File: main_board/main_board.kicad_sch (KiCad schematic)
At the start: 56 parts, among them J1 USB4105-GF-A-060, J2 Conn_01x06_Pin, Q3 NX3008PBK,215, U1 SSD1306, U2 ESP32-S2-SOLO, U3 TLV62568PDRLT, U4 MCP73832, U5 DW01, U6 8205A, U7 MAX17055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

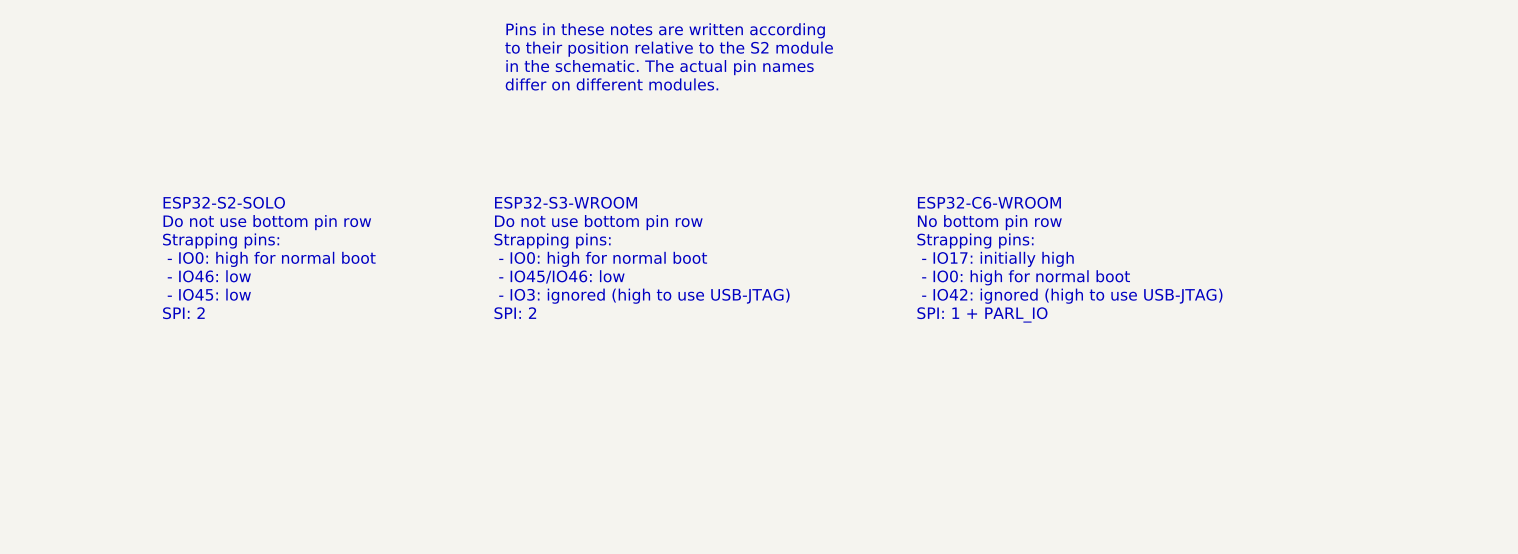
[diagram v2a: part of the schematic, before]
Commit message: Add a note about LP GPIO ranges
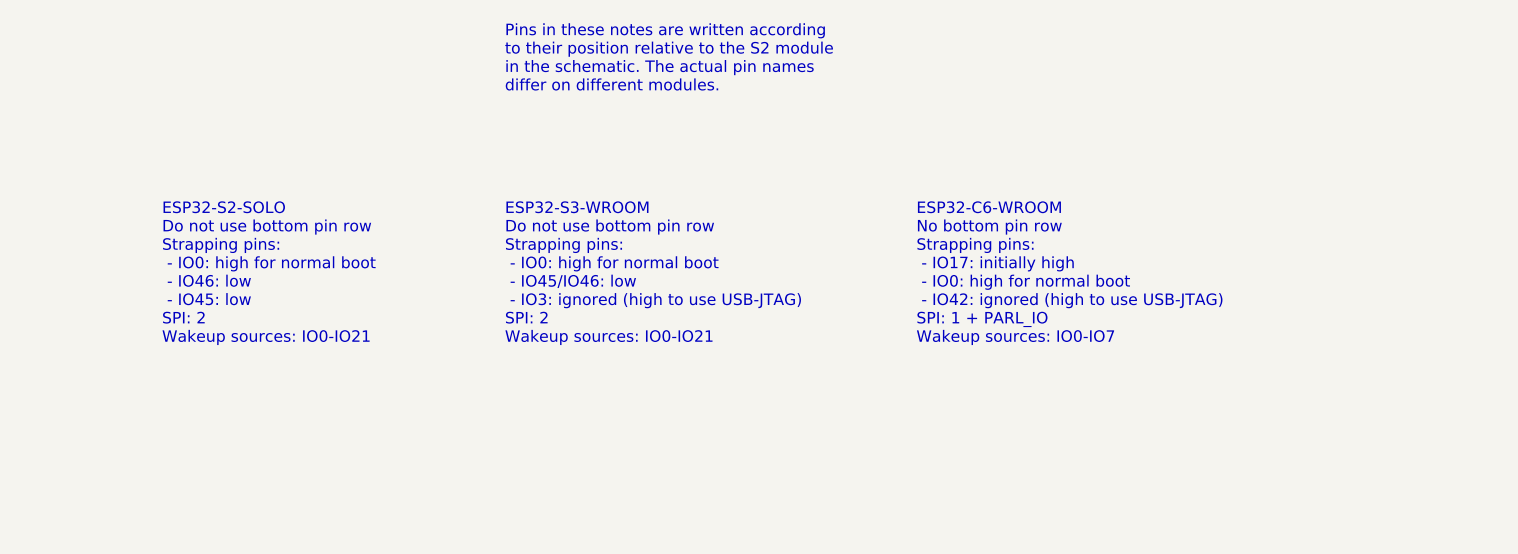
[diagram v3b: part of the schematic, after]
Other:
- note added: "ESP32-C6-WROOM No bottom pin row Strapping pins: - IO17: initially high - IO0: high for normal boot - IO42: ignored (high to use USB-JTAG) SPI: 1 + PARL_IO Wakeup sources: IO0-IO7"
- note added: "ESP32-S2-SOLO Do not use bottom pin row Strapping pins: - IO0: high for normal boot - IO46: low - IO45: low SPI: 2 Wakeup sources: IO0-IO21"
- note added: "ESP32-S3-WROOM Do not use bottom pin row Strapping pins: - IO0: high for normal boot - IO45/IO46: low - IO3: ignored (high to use USB-JTAG) SPI: 2 Wakeup sources: IO0-IO21"
- note removed: "ESP32-C6-WROOM No bottom pin row Strapping pins: - IO17: initially high - IO0: high for normal boot - IO42: ignored (high to use USB-JTAG) SPI: 1 + PARL_IO"
- note removed: "ESP32-S2-SOLO Do not use bottom pin row Strapping pins: - IO0: high for normal boot - IO46: low - IO45: low SPI: 2"
- note removed: "ESP32-S3-WROOM Do not use bottom pin row Strapping pins: - IO0: high for normal boot - IO45/IO46: low - IO3: ignored (high to use USB-JTAG) SPI: 2"
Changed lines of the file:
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@@
     (effects (font (size 1.27 1.27)) (justify left bottom))
   )
-  (text "ESP32-C6-WROOM\nNo bottom pin row\nStrapping pins:\n - IO17: initially high\n - IO0: high for normal boot\n - IO42: ignored (high to use USB-JTAG)\nSPI: 1 + PARL_IO"
-    (at 161.29 -25.4 0)
+  (text "ESP32-C6-WROOM\nNo bottom pin row\nStrapping pins:\n - IO17: initially high\n - IO0: high for normal boot\n - IO42: ignored (high to use USB-JTAG)\nSPI: 1 + PARL_IO\nWakeup sources: IO0-IO7"
+    (at 161.29 -22.86 0)
     (effects (font (size 1.27 1.27)) (justify left bottom))
   )
@@
     (effects (font (size 1.27 1.27)) (justify left bottom))
   )
-  (text "ESP32-S3-WROOM\nDo not use bottom pin row\nStrapping pins:\n - IO0: high for normal boot\n - IO45/IO46: low\n - IO3: ignored (high to use USB-JTAG)\nSPI: 2"
-    (at 114.3 -25.4 0)
+  (text "ESP32-S3-WROOM\nDo not use bottom pin row\nStrapping pins:\n - IO0: high for normal boot\n - IO45/IO46: low\n - IO3: ignored (high to use USB-JTAG)\nSPI: 2\nWakeup sources: IO0-IO21"
+    (at 115.57 -22.86 0)
     (effects (font (size 1.27 1.27)) (justify left bottom))
   )
@@
     (effects (font (size 1.27 1.27)) (justify left bottom))
   )
-  (text "ESP32-S2-SOLO\nDo not use bottom pin row\nStrapping pins:\n - IO0: high for normal boot\n - IO46: low\n - IO45: low\nSPI: 2"
-    (at 77.47 -25.4 0)
+  (text "ESP32-S2-SOLO\nDo not use bottom pin row\nStrapping pins:\n - IO0: high for normal boot\n - IO46: low\n - IO45: low\nSPI: 2\nWakeup sources: IO0-IO21"
+    (at 77.47 -22.86 0)
     (effects (font (size 1.27 1.27)) (justify left bottom))
   )

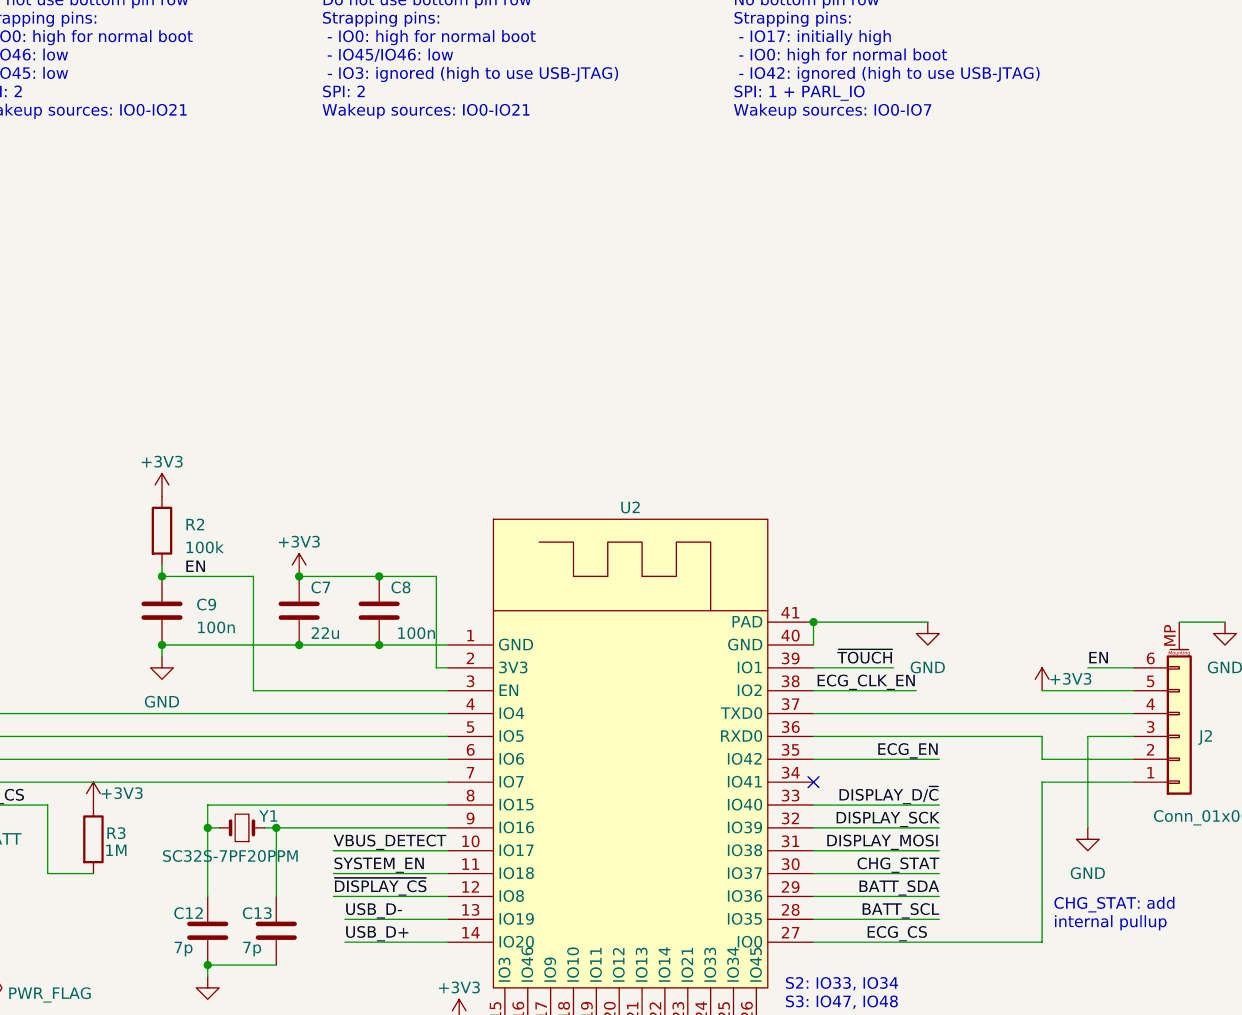
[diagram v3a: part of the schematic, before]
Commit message: Fix #36: swap VBUS_DETECT and DISPLAY_CS
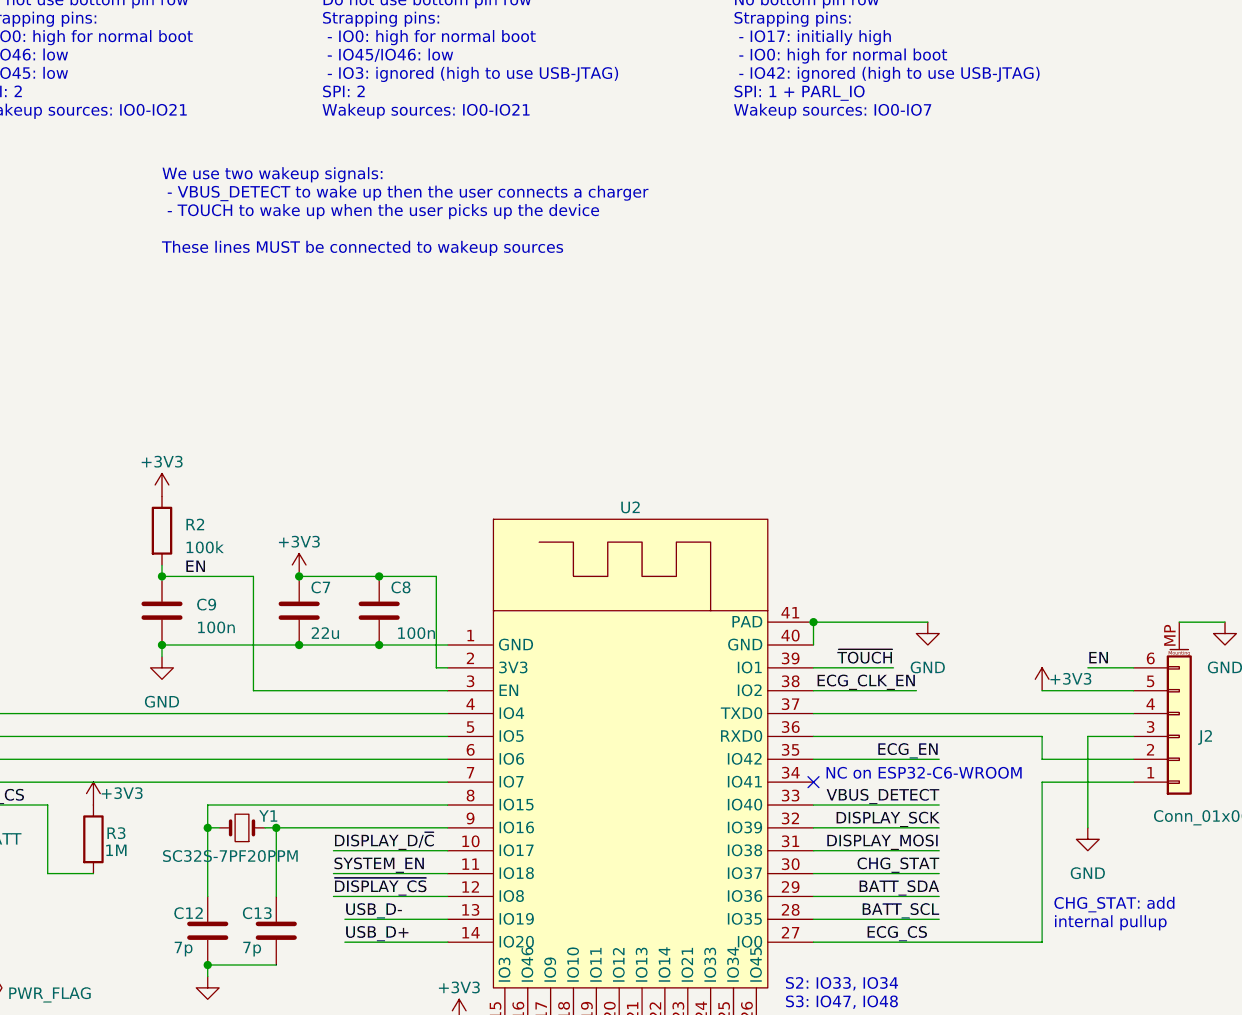
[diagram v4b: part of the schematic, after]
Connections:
- net DISPLAY_D/~{C}: now also U2.10 (IO17); no longer U2.33 (IO40)
- net VBUS_DETECT: now also U2.33 (IO40); no longer U2.10 (IO17)
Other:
- note added: "NC on ESP32-C6-WROOM"
- note added: "We use two wakeup signals: - VBUS_DETECT to wake up then the user connects a charger - TOUCH to wake up when the user picks up the device These lines MUST be connected to wakeup sources"
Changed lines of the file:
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@@
     (fill (type none))
+  )
+  (text "We use two wakeup signals:\n - VBUS_DETECT to wake up then the user connects a charger\n - TOUCH to wake up when the user picks up the device\n\nThese lines MUST be connected to wakeup sources"
+    (at 97.79 -7.62 0)
+    (effects (font (size 1.27 1.27)) (justify left bottom))
   )
   (text "USB-C" (at 207.01 161.29 0)
@@
   (text "ESP32-S3-WROOM\nDo not use bottom pin row\nStrapping pins:\n - IO0: high for normal boot\n - IO45/IO46: low\n - IO3: ignored (high to use USB-JTAG)\nSPI: 2\nWakeup sources: IO0-IO21"
     (at 115.57 -22.86 0)
+    (effects (font (size 1.27 1.27)) (justify left bottom))
+  )
+  (text "NC on ESP32-C6-WROOM" (at 171.45 50.8 0)
     (effects (font (size 1.27 1.27)) (justify left bottom))
   )
@@
     (effects (font (size 1.27 1.27)) (justify left bottom))
   )
-  (label "DISPLAY_D{slash}~{C}" (at 184.15 53.34 180) (fields_autoplaced)
-    (effects (font (size 1.27 1.27)) (justify right bottom))
+  (label "DISPLAY_D{slash}~{C}" (at 116.84 58.42 0) (fields_autoplaced)
+    (effects (font (size 1.27 1.27)) (justify left bottom))
   )
   (label "USB_D+" (at 208.28 135.89 180) (fields_autoplaced)
@@
     (effects (font (size 1.27 1.27)) (justify left bottom))
   )
-  (label "VBUS_DETECT" (at 116.84 58.42 0) (fields_autoplaced)
-    (effects (font (size 1.27 1.27)) (justify left bottom))
+  (label "VBUS_DETECT" (at 184.15 53.34 180) (fields_autoplaced)
+    (effects (font (size 1.27 1.27)) (justify right bottom))
   )
   (label "DISPLAY_MOSI" (at 184.15 58.42 180) (fields_autoplaced)
